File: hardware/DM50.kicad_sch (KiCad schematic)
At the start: 106 parts, among them J1 ST-LINK, J2 USB_C_Receptacle_USB2.0_14P, J4 Conn_01x04, Q1 MMBT3904, SW1 SW_SPST, SW10 BT_SMD, SW11 BT_SMD, SW12 BT_SMD, SW13 BT_SMD, SW14 BT_SMD, SW15 BT_SMD, SW16 BT_SMD, SW17 BT_SMD, SW18 BT_SMD, SW19 BT_SMD, SW2 BT_SMD, SW20 BT_SMD, SW21 BT_SMD, SW22 BT_SMD, SW23 BT_SMD, SW24 BT_SMD, SW25 BT_SMD, SW26 BT_SMD, SW27 BT_SMD, SW28 BT_SMD, SW29 BT_SMD, SW3 BT_SMD, SW30 BT_SMD, SW31 BT_SMD, SW32 BT_SMD, SW33 BT_SMD, SW34 BT_SMD, SW35 BT_SMD, SW36 BT_SMD, SW37 BT_SMD, SW38 BT_SMD, SW39 BT_SMD, SW4 BT_SMD, SW40 BT_SMD, SW41 BT_SMD, SW42 SW_SPST, SW43 BT_SMD, SW44 BT_SMD, SW45 BT_SMD, SW46 BT_SMD, SW47 BT_SMD, SW48 BT_SMD, SW49 BT_SMD, SW5 BT_SMD, SW50 BT_SMD, SW51 BT_SMD, SW52 BT_SMD, SW6 BT_SMD, SW7 BT_SMD, SW8 BT_SMD, SW9 BT_SMD, U1 EA_DOGL128X-6, U2 STM32U535CBT6, U3 AT25SF641, U4 USBLC6-2SC6, U5 ADP2108AUJ-3.3, U6 MCP73831-2-OT, Y1 32768

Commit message: LiPO CONNECTOR
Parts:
- added D4: schottky, Diode_SMD:D_SOD-323, symbol Device:D_Schottky
- added JP1: LiPO, Jumper:SolderJumper-2_P1.3mm_Bridged_RoundedPad1.0x1.5mm, symbol Jumper:SolderJumper_2_Open
- BT1, BT2: value AA -> AAA
- J4: value Conn_01x04 -> LiPO 3,7V; footprint DM50:CONN_S2B-ZR-SM4A-TFLFSN_JST -> DM50:CONN_S2B-PH-K-S_JST; symbol Connector_Generic:Conn_01x04 -> Connector_Generic:Conn_01x02
- U6: value MCP73831-2-OT -> MCP73831
- Y1: footprint Crystal:Crystal_SMD_MicroCrystal_CM9V-T1A-2Pin_1.6x1.0mm -> DM50:XTAL_ABS05-32.768KHZ-9-T
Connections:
- net 3.3V: now also U2.1 (VBAT)
- net GND: now also J4.1 (Pin_1); no longer J4.2 (Pin_2), J4.3 (Pin_3), J4.4 (Pin_4)
- net VBUS: now also JP1.2 (B); no longer U6.4 (V_{DD})
- net VINPUT: now also D4.1 (K)
- removed net VBAT: BT1.1 (+), C23.1, D2.1, J4.1 (Pin_1), U2.1 (VBAT), U6.3 (V_{BAT})
- new net: JP1.1 (A), U6.4 (V_{DD})
- new net: BT1.1 (+), D2.1
- new net: C23.1, D4.2 (A), J4.2 (Pin_2), U6.3 (V_{BAT})
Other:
- note added: "2xAAA"
- note removed: "Display Visions EA DOGL128L-6 (L is reflective, without leds) https://www.digikey.es/es/products/detail/display-visions/EA-DOGL128L-6/4896695 Regulators LD3985, TPS61222TCK, Battery: https://www.digikey.es/es/products/detail/keystone-electronics/54/2254090"
- note removed: "LiPO OR 2xAA"
- moved on the sheet: C23

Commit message: pcb changes
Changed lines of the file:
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@@
 		)
 		(property "Value" "AT25SF641"
-			(at 272.542 109.22 90)
+			(at 268.478 116.84 0)
 			(effects
 				(font

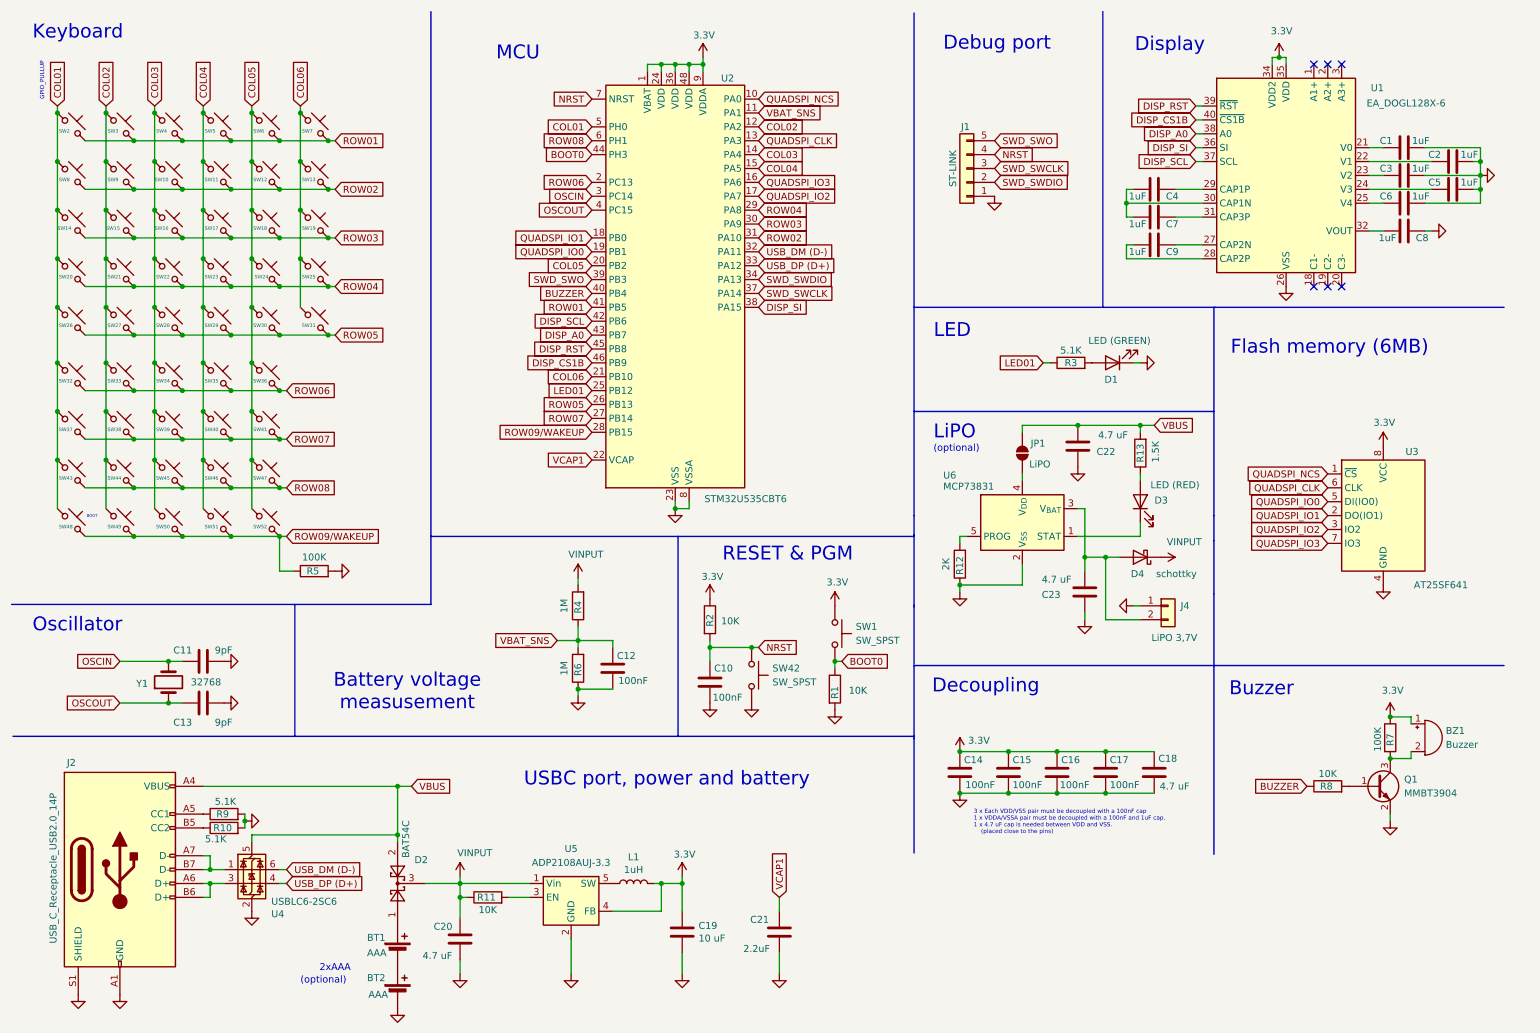
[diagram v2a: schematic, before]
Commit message: LiPO charging sensor
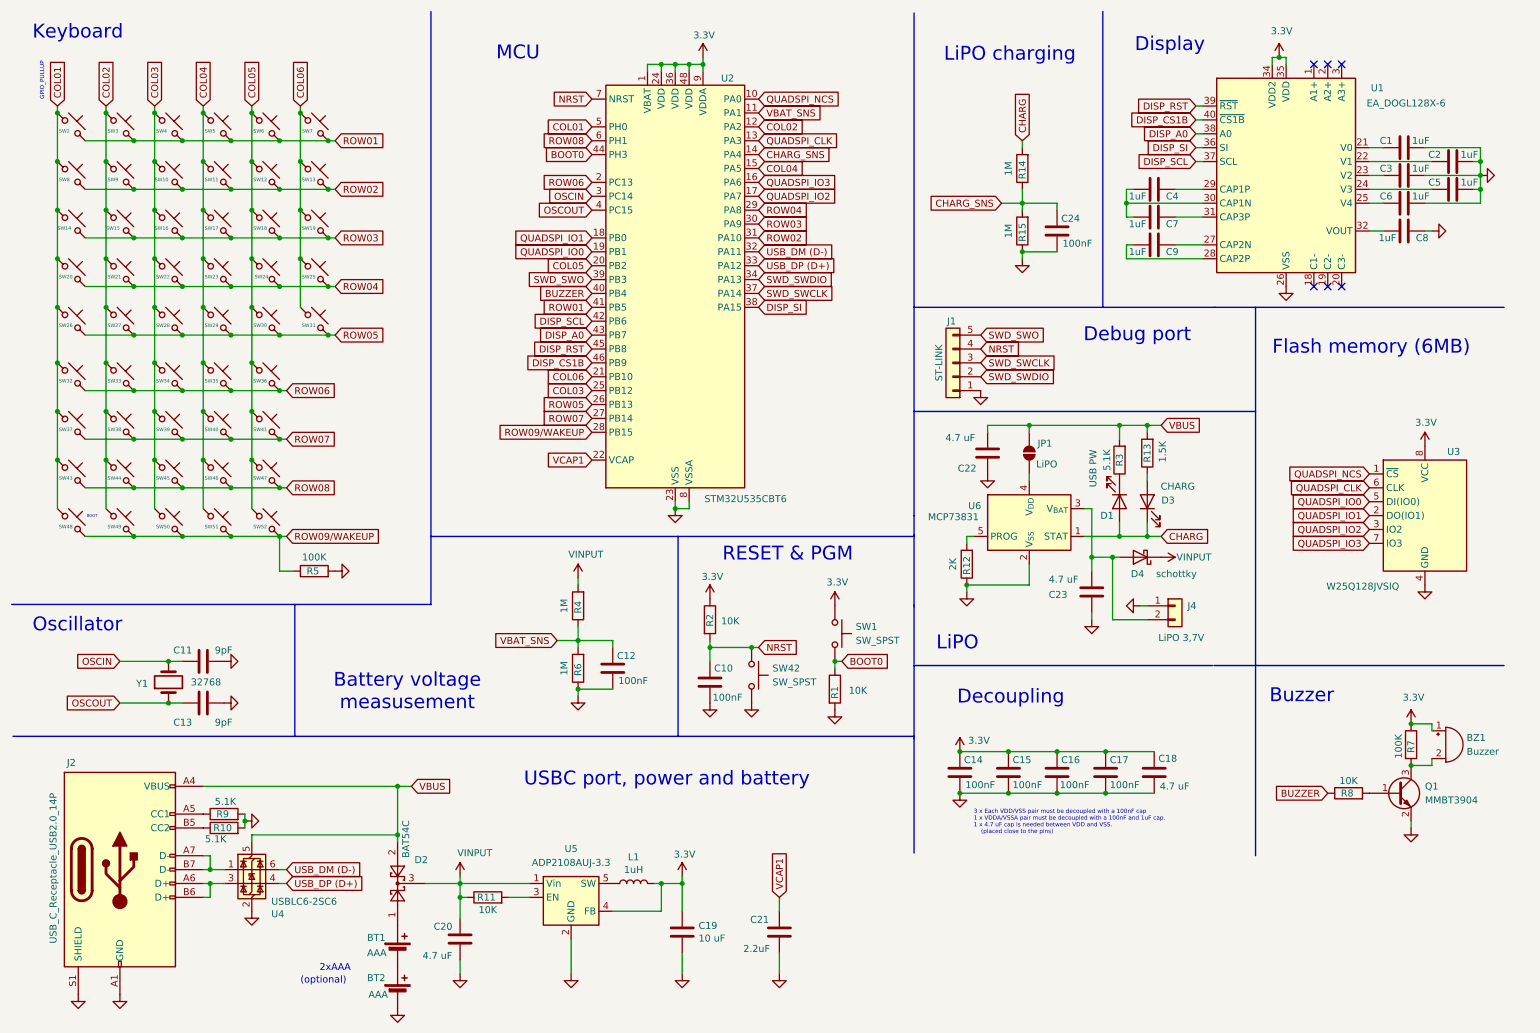
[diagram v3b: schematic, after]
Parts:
- added C24: 100nF, Capacitor_SMD:C_0603_1608Metric, symbol Device:C
- added R14, R15: 1M, Resistor_SMD:R_0603_1608Metric, symbol Device:R
- D1: value LED (GREEN) -> USB PW
- D3: value LED (RED) -> CHARG
- U3: value AT25SF641 -> W25Q128JVSIQ
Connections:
- net COL03: now also U2.25 (PB12); no longer U2.14 (PA4)
- net GND: now also C24.2, R15.1; no longer D1.1 (K)
- net VBUS: now also R3.2
- net CHARG: now reaches D1.2 (A)
- net CHARG: now also D3.1 (K), U6.1 (STAT), R14.2; no longer R3.2
- net LED01: no longer names the net of R3.1
- net LED01: now also D1.1 (K); no longer U2.25 (PB12)
- new net CHARG_SNS: C24.1, R14.1, R15.2, U2.14 (PA4)
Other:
- note added: "LiPO charging"
- note removed: "LED"
- moved on the sheet: BZ1, C22, C23, D1, D3, J1, J4, JP1, Q1, R12, R13, R3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

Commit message: pcb changes
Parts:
- removed U2: STM32U535CBT6, Package_QFP:LQFP-48_7x7mm_P0.5mm, symbol MCU_ST_STM32U5:STM32U535CBTx
- added U2: STM32U575CITx, Package_QFP:LQFP-48_7x7mm_P0.5mm, symbol MCU_ST_STM32U5:STM32U575CITx
- SW1, SW42: footprint Button_Switch_SMD:SW_SPST_TL3342 -> Button_Switch_SMD:SW_SPST_CK_KMS2xxG
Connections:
- net 3.3V: now also U2.1 (VBAT), U2.24 (VDD), U2.36 (VDD), U2.48 (VDD), U2.9 (VDDA)
- net BOOT0: now also U2.44 (PH3)
- net BUZZER: now also U2.40 (PB4)
- net CHARG_SNS: now also U2.14 (PA4)
- net COL01: now also U2.5 (PH0)
- net COL02: now also U2.12 (PA2)
- net COL03: now also U2.25 (PB12)
- net COL04: now also U2.15 (PA5)
- net COL05: now also U2.20 (PB2)
- net COL06: now also U2.21 (PB10)
- net DISP_A0: now also U2.43 (PB7)
- net DISP_CS1B: now also U2.46 (PB9)
- net DISP_RST: now also U2.45 (PB8)
- net DISP_SCL: now also U2.42 (PB6)
- net DISP_SI: now also U2.38 (PA15)
- net GND: now also U2.23 (VSS), U2.35 (VSS), U2.47 (VSS), U2.8 (VSSA)
- net NRST: now also U2.7 (NRST)
- net OSCIN: now also U2.3 (PC14)
- net OSCOUT: now also U2.4 (PC15)
- net QUADSPI_CLK: now also U2.13 (PA3)
- net QUADSPI_IO0: now also U2.19 (PB1)
- net QUADSPI_IO1: now also U2.18 (PB0)
- net QUADSPI_IO2: now also U2.17 (PA7)
- net QUADSPI_IO3: now also U2.16 (PA6)
- net QUADSPI_NCS: now also U2.10 (PA0)
- net ROW01: now also U2.41 (PB5)
- net ROW02: now also U2.31 (PA10)
- net ROW03: now also U2.30 (PA9)
- net ROW04: now also U2.29 (PA8)
- net ROW05: now also U2.26 (PB13)
- net ROW06: now also U2.2 (PC13)
- net ROW07: now also U2.27 (PB14)
- net ROW08: now also U2.6 (PH1)
- net ROW09/WAKEUP: now also U2.28 (PB15)
- net SWD_SWCLK: now also U2.37 (PA14)
- net SWD_SWDIO: now also U2.34 (PA13)
- net SWD_SWO: now also U2.39 (PB3)
- net USB_DM (D-): now also U2.32 (PA11)
- net USB_DP (D+): now also U2.33 (PA12)
- net VBAT_SNS: now also U2.11 (PA1)
- net VCAP1: now also U2.22 (VCAP)
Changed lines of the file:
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@@
 	)
 	(symbol
-		(lib_id "MCU_ST_STM32U5:STM32U535CBTx")
-		(at 133.35 63.5 0)
-		(unit 1)
-		(exclude_from_sim no)
-		(in_bom yes)
-		(on_board yes)
-		(dnp no)
-		(property "Reference" "U2"
-			(at 141.732 24.13 0)
-			(effects
-				(font
-					(size 1.27 1.27)
-				)
-				(justify left)
-			)
-		)
-		(property "Value" "STM32U535CBT6"
-			(at 138.684 101.092 0)
-			(effects
-				(font
-					(size 1.27 1.27)
-				)
-				(justify left)
-			)
-		)
-		(property "Footprint" "Package_QFP:LQFP-48_7x7mm_P0.5mm"
-			(at 120.65 99.06 0)
-			(effects
-				(font
-					(size 1.27 1.27)
-				)
-				(justify right)
-				(hide yes)
-			)
-		)
-		(property "Datasheet" "https://www.digikey.es/es/products/detail/stmicroelectronics/STM32U545CET6Q/20412791"
-			(at 133.35 63.5 0)
-			(effects
-				(font
-					(size 1.27 1.27)
-				)
-				(hide yes)
-			)
-		)
-		(property "Description" "STMicroelectronics Arm Cortex-M33 MCU, 128KB flash, 274KB RAM, 37 GPIO, LQFP48"
-			(at 133.35 63.5 0)
-			(effects
-				(font
-					(size 1.27 1.27)
-				)
-				(hide yes)
-			)
-		)
-		(pin "19"
-		)
-		(pin "2"
-		)
-		(pin "17"
-		)
-		(pin "18"
-		)
-		(pin "11"
-		)
-		(pin "20"
-		)
-		(pin "21"
-		)
-		(pin "13"
-		)
-		(pin "15"
-		)
-		(pin "16"
-		)
-		(pin "22"
-		)
-		(pin "23"
-		)
-		(pin "24"
-		)
-		(pin "25"
-		)
-		(pin "26"
-		)
-		(pin "27"
-		)
-		(pin "28"
-		)
-		(pin "29"
-		)
-		(pin "3"
-		)
-		(pin "30"
-		)
-		(pin "31"
-		)
-		(pin "32"
-		)
-		(pin "33"
-		)
-		(pin "34"
-		)
-		(pin "35"
-		)
-		(pin "36"
-		)
-		(pin "37"
-		)
-		(pin "38"
-		)
-		(pin "39"
-		)
-		(pin "4"
-		)
-		(pin "40"
-		)
-		(pin "41"
-		)
-		(pin "42"
-		)
-		(pin "43"
-		)
-		(pin "44"
-		)
-		(pin "45"
-		)
-		(pin "46"
-		)
-		(pin "47"
-		)
-		(pin "48"
-		)
-		(pin "5"
-		)
-		(pin "6"
-		)
-		(pin "7"
-		)
-		(pin "8"
-		)
-		(pin "9"
-		)
-		(pin "1"
-		)
-		(pin "12"
-		)
-		(pin "10"
-		)
-		(pin "14"
-		)
-		(instances
-			(project "DM50"
-				(path "/191bb639-a0ba-4e03-a281-e8ebad1939b8"
-					(reference "U2")
-					(unit 1)
-				)
-			)
-		)
-	)
-	(symbol
 		(lib_id "Switch:SW_Push_45deg")
 		(at 67.31 68.58 0)
@@
 			)
 		)
-		(property "Footprint" "Button_Switch_SMD:SW_SPST_TL3342"
+		(property "Footprint" "Button_Switch_SMD:SW_SPST_CK_KMS2xxG"
 			(at 152.4 133.35 0)
 			(effects
@@
 			)
 		)
-		(property "Footprint" "Button_Switch_SMD:SW_SPST_TL3342"
+		(property "Footprint" "Button_Switch_SMD:SW_SPST_CK_KMS2xxG"
 			(at 167.64 125.73 0)
 			(effects
@@
 					(unit 1)
 				)
+			)
+		)
+	)
+	(symbol
+		(lib_id "MCU_ST_STM32U5:STM32U575CITx")
+		(at 133.35 63.5 0)
+		(unit 1)
+		(exclude_from_sim no)
+		(in_bom yes)
+		(on_board yes)
+		(dnp no)
+		(fields_autoplaced yes)
+		(property "Reference" "U2"
+			(at 138.0841 101.6 0)
+			(effects
+				(font
+					(size 1.27 1.27)
+				)
+				(justify left)
+			)
+		)
+		(property "Value" "STM32U575CITx"
+			(at 138.0841 104.14 0)
+			(effects
+				(font
+					(size 1.27 1.27)
+				)
+				(justify left)
+			)
+		)
+		(property "Footprint" "Package_QFP:LQFP-48_7x7mm_P0.5mm"
+			(at 120.65 99.06 0)
+			(effects
+				(font
+					(size 1.27 1.27)
+				)
+				(justify right)
+				(hide yes)
+			)
+		)
+		(property "Datasheet" "https://www.st.com/resource/en/datasheet/stm32u575ci.pdf"
+			(at 133.35 63.5 0)
+			(effects
+				(font
+					(size 1.27 1.27)
+				)
+				(hide yes)
+			)
+		)
+		(property "Description" "STMicroelectronics Arm Cortex-M33 MCU, 2048KB flash, 786KB RAM, 160 MHz, 1.71-3.6V, 37 GPIO, LQFP48"
+			(at 133.35 63.5 0)
+			(effects
+				(font
+					(size 1.27 1.27)
+				)
+				(hide yes)
+			)
+		)
+		(pin "24"
+		)
+		(pin "23"
+		)
+		(pin "45"
+		)
+		(pin "46"
+		)
+		(pin "17"
+		)
+		(pin "33"
+		)
+		(pin "34"
+		)
+		(pin "35"
+		)
+		(pin "36"
+		)
+		(pin "20"
+		)
+		(pin "37"
+		)
+		(pin "38"
+		)
+		(pin "11"
+		)
+		(pin "12"
+		)
+		(pin "39"
+		)
+		(pin "40"
+		)
+		(pin "1"
+		)
+		(pin "47"
+		)
+		(pin "48"
+		)
+		(pin "5"
+		)
+		(pin "13"
+		)
+		(pin "31"
+		)
+		(pin "32"
+		)
+		(pin "3"
+		)
+		(pin "30"
+		)
+		(pin "9"
+		)
+		(pin "14"
+		)
+		(pin "6"
+		)
+		(pin "7"
+		)
+		(pin "8"
+		)
+		(pin "22"
+		)
+		(pin "16"
+		)
+		(pin "18"
+		)
+		(pin "25"
+		)
+		(pin "43"
+		)
+		(pin "44"
+		)
+		(pin "19"
+		)
+		(pin "10"
+		)
+		(pin "41"
+		)
+		(pin "42"
+		)
+		(pin "21"
+		)
+		(pin "2"
+		)
+		(pin "4"
+		)
+		(pin "15"
+		)
+		(pin "26"
+		)
+		(pin "27"
+		)
+		(pin "28"
+		)
+		(pin "29"
+		)
+		(instances
+			(project ""
+				(path "/191bb639-a0ba-4e03-a281-e8ebad1939b8"
+					(reference "U2")
+					(unit 1)
+				)

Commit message: add jtag connector
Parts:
- J1: footprint DM50:JST_CON_SMD -> DM50:SAMTEC-SMH-105-02-X-S
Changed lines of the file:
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@@
 			)
 		)
-		(property "Footprint" "DM50:JST_CON_SMD"
+		(property "Footprint" "DM50:SAMTEC-SMH-105-02-X-S"
 			(at 184.15 76.2 0)
 			(effects

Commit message: pcb changes
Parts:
- BT1, BT2: now left out of the parts list
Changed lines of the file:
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@@
 		(unit 1)
 		(exclude_from_sim no)
-		(in_bom yes)
+		(in_bom no)
 		(on_board yes)
 		(dnp no)
@@
 		(unit 1)
 		(exclude_from_sim no)
-		(in_bom yes)
-		(on_board yes)
-		(dnp no)
+		(in_bom no)
+		(on_board yes)
+		(dnp no)
